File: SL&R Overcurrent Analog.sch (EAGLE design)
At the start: 22 parts, among them IC1 TLC393CPN, IC2 CSLA2CFTH, Q1 SUP75P0307, Q2 SUP75P0307, X1 J1, X2 J2, X3 J3

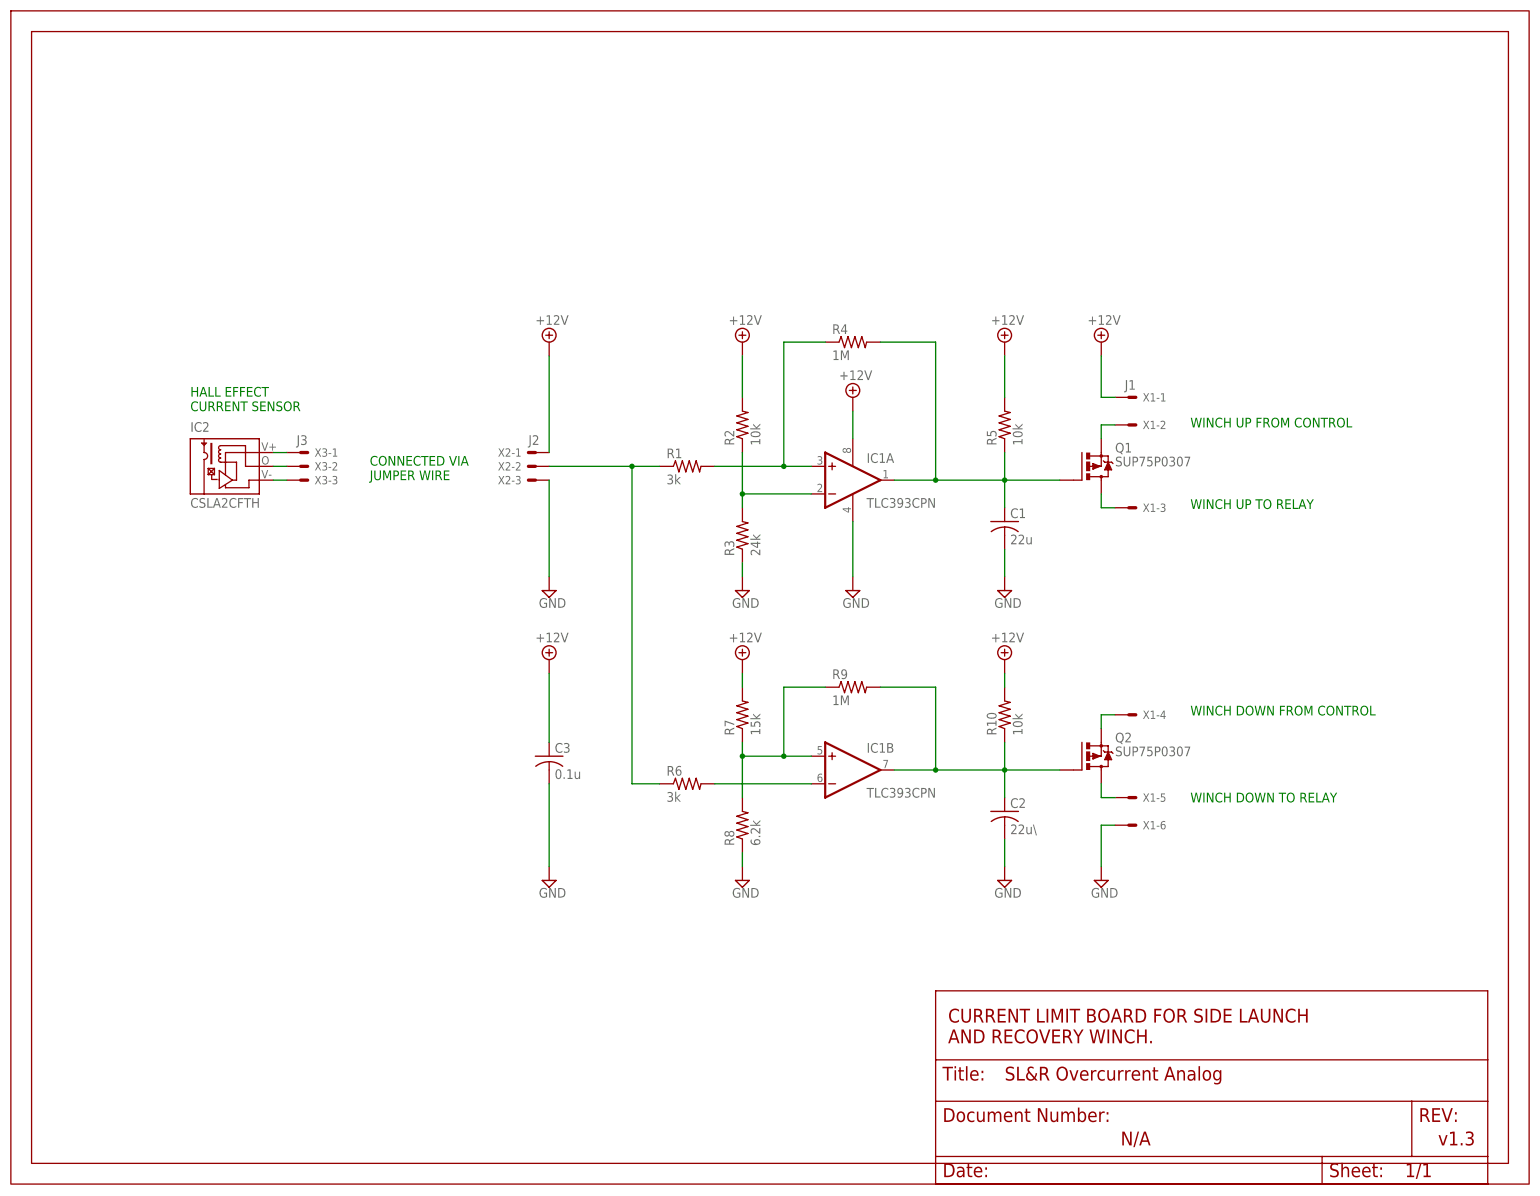
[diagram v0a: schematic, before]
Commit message: Indicators, adjustable limits, test points
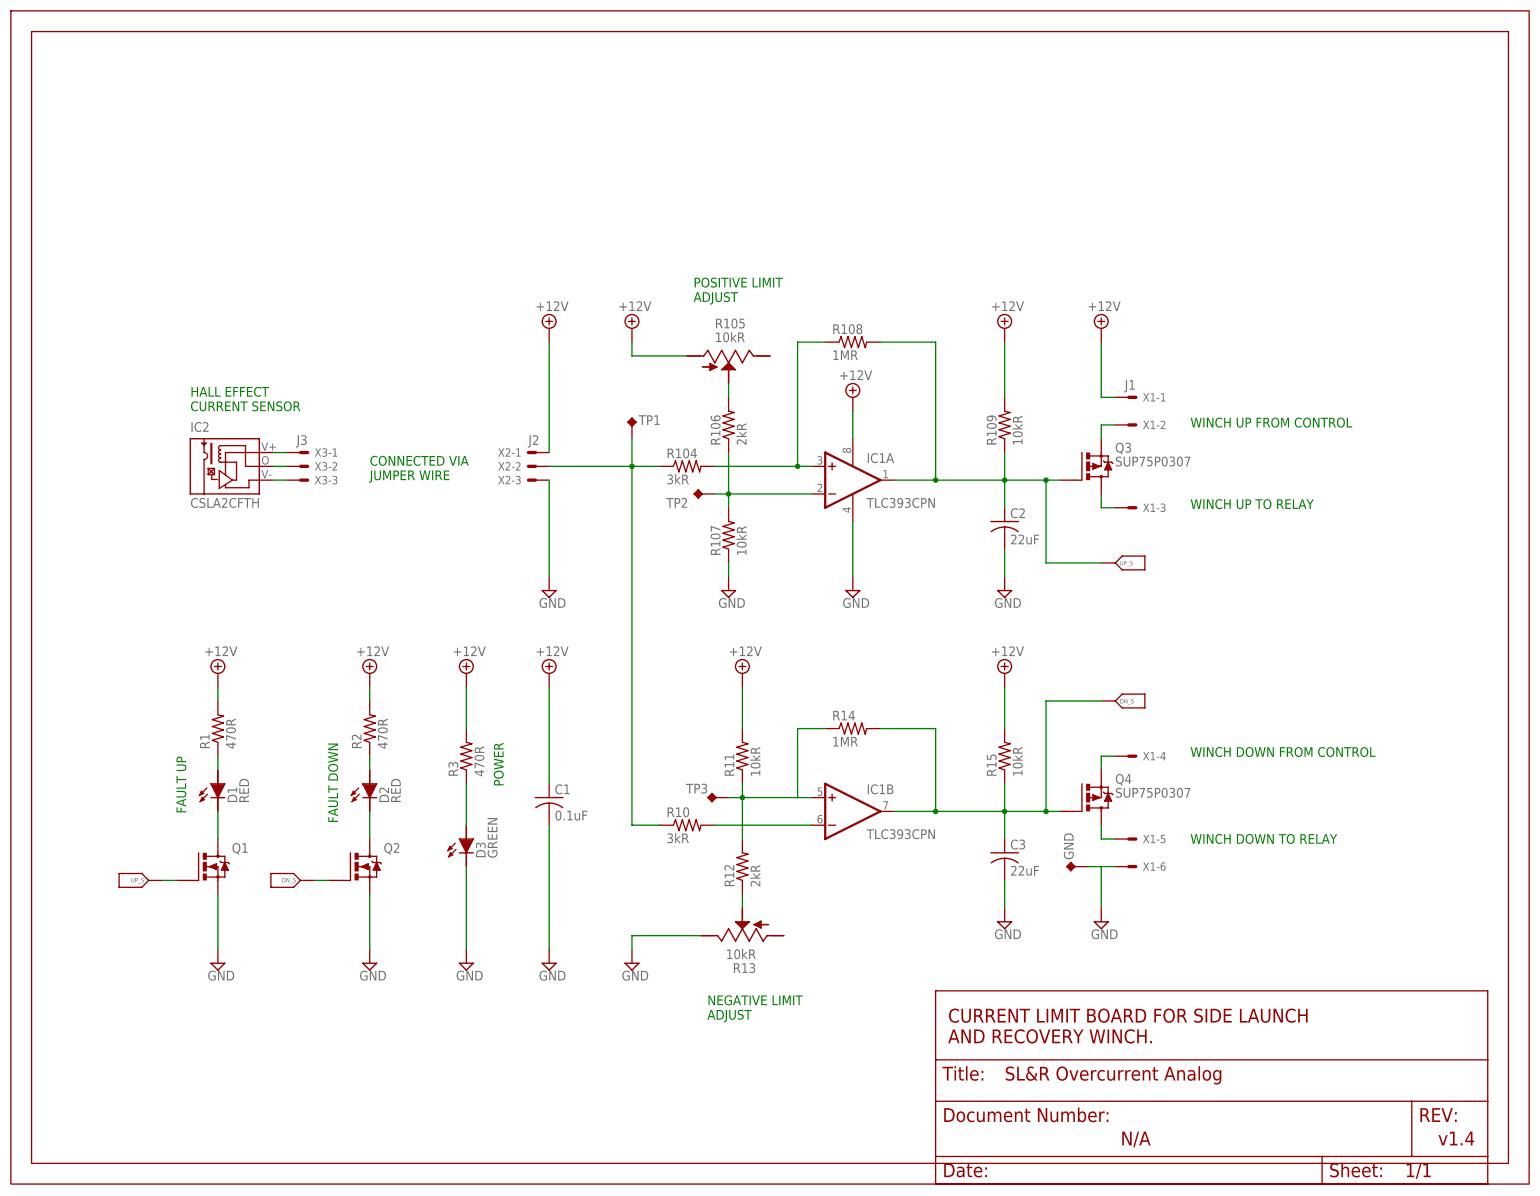
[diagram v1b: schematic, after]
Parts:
- removed R6: 3k, Overcurrent Detect:RESISTOR-US0204/7
- removed R7: 15k, Overcurrent Detect:RESISTOR-US0204/7
- removed R8: 6.2k, Overcurrent Detect:RESISTOR-US0204/7
- removed R9: 1M, Overcurrent Detect:RESISTOR-US0204/7
- added D1, D2: RED, SL&R Overcurrent Analog:LED
- added D3: GREEN, SL&R Overcurrent Analog:LED
- added GND, TP1, TP2, TP3: TEST_POINT, SL&R Overcurrent Analog:TEST_POINT
- added Q3, Q4: SUP75P0307, Overcurrent Detect:SUP75P0307
- added R104: 3kR, Overcurrent Detect:RESISTOR-US0204/7
- added R105, R13: 10kR, SL&R Overcurrent Analog:POT
- added R106, R12: 2kR, Overcurrent Detect:RESISTOR-US0204/7
- added R107, R11, R15: 10kR, Overcurrent Detect:RESISTOR-US0204/7
- added R14: 1MR, Overcurrent Detect:RESISTOR-US0204/7
- C1: value 22u -> 0.1uF; device Overcurrent Detect:CAPACITOR-US025-050X050 -> Overcurrent Detect:CAPACITOR-US
- C2: value 22u\ -> 22uF
- C3: value 0.1u -> 22uF; device Overcurrent Detect:CAPACITOR-US -> Overcurrent Detect:CAPACITOR-US025-050X050
- Q1, Q2: value SUP75P0307 -> (none); device Overcurrent Detect:SUP75P0307 -> SL&R Overcurrent Analog:2N7000
- R1: value 3k -> 470R; device Overcurrent Detect:RESISTOR-US0204/7 -> SL&R Overcurrent Analog:RESISTOR-US0204/7
- R10: value 10k -> 3kR
- R108: value 1M -> 1MR
- R109: value 10k -> 10kR
- R2: value 10k -> 470R; device Overcurrent Detect:RESISTOR-US0204/7 -> SL&R Overcurrent Analog:RESISTOR-US0204/7
- R3: value 24k -> 470R; device Overcurrent Detect:RESISTOR-US0204/7 -> SL&R Overcurrent Analog:RESISTOR-US0204/7
- renumbered R4 to R108, R5 to R109
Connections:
- new net N$16: D1.C, Q1.D
- new net N$17: D2.A, R2.1
- new net N$18: D2.C, Q2.D
- new net N$19: D3.A, R3.1
- new net N$20: R105.2, R106.2
- new net N$22: R12.1, R13.2
- new net N$3: D1.A, R1.1
- net +12V: now also C1.1, R1.2, R105.3, R11.2, R15.2, R3.2; no longer C3.1, R10.2, R7.2
- net GND: now also D3.C, GND.TP, Q1.S, Q2.S, R107.1, R13.1; no longer R3.1, R8.1
- net N$1: now also R104.2; no longer R1.2
- net N$10: now also Q4.S; no longer Q2.S
- net N$11: now also Q4.D; no longer Q2.D
- net N$15: now also R10.1, R104.1, TP1.TP; no longer R1.1, R6.1
- net N$2: now also R106.1, R107.2, TP2.TP; no longer R2.1, R3.2
- net N$4: now also R10.2; no longer R6.2
- net N$5: now also R11.1, R12.2, R14.1, TP3.TP; no longer R7.1, R8.2, R9.1
- net N$6: now also C2.1, Q3.G; no longer C1.1
- net N$7: now also C3.1, Q4.G, R14.2, R15.1; no longer C2.1, R10.1, R9.2
- net N$8: now also Q3.S; no longer Q1.S
- net N$9: now also Q3.D; no longer Q1.D
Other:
- note added: "FAULT DOWN"
- note added: "FAULT UP"
- note added: "NEGATIVE LIMIT ADJUST"
- note added: "POSITIVE LIMIT ADJUST"
- note added: "POWER"
- note added: "v1.4"
- note removed: "v1.3"
- moved on the sheet: C1, C2, C3, IC1B, R1, R10, R2, R3, X1-4, X1-5, X1-6

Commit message: Minor updates
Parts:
- renumbered R104 to R4, R105 to R5, R106 to R6, R107 to R7, R108 to R8, R109 to R9
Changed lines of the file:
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@@
 <part name="IC2" library="Overcurrent Detect" deviceset="CSLA2CF" device="TH"/>
 <part name="IC1" library="Overcurrent Detect" deviceset="TLC393CP" device="N"/>
-<part name="R104" library="Overcurrent Detect" deviceset="RESISTOR-US" device="0204/7" value="3kR"/>
-<part name="R106" library="Overcurrent Detect" deviceset="RESISTOR-US" device="0204/7" value="2kR"/>
-<part name="R108" library="Overcurrent Detect" deviceset="RESISTOR-US" device="0204/7" value="1MR"/>
-<part name="R109" library="Overcurrent Detect" deviceset="RESISTOR-US" device="0204/7" value="10kR"/>
+<part name="R4" library="Overcurrent Detect" deviceset="RESISTOR-US" device="0204/7" value="3kR"/>
+<part name="R6" library="Overcurrent Detect" deviceset="RESISTOR-US" device="0204/7" value="2kR"/>
+<part name="R8" library="Overcurrent Detect" deviceset="RESISTOR-US" device="0204/7" value="1MR"/>
+<part name="R9" library="Overcurrent Detect" deviceset="RESISTOR-US" device="0204/7" value="10kR"/>
 <part name="R10" library="Overcurrent Detect" deviceset="RESISTOR-US" device="0204/7" value="3kR"/>
 <part name="R12" library="Overcurrent Detect" deviceset="RESISTOR-US" device="0204/7" value="2kR"/>
@@
 <part name="LABEL3" library="SL&amp;R Overcurrent Analog" deviceset="WIRE_LABEL" device="" value="UP_S"/>
 <part name="LABEL4" library="SL&amp;R Overcurrent Analog" deviceset="WIRE_LABEL" device="" value="DN_S"/>
-<part name="R105" library="SL&amp;R Overcurrent Analog" deviceset="POT" device="" value="10kR"/>
+<part name="R5" library="SL&amp;R Overcurrent Analog" deviceset="POT" device="" value="10kR"/>
 <part name="R13" library="SL&amp;R Overcurrent Analog" deviceset="POT" device="" value="10kR"/>
 <part name="Q1" library="SL&amp;R Overcurrent Analog" deviceset="2N7000" device=""/>
 <part name="Q2" library="SL&amp;R Overcurrent Analog" deviceset="2N7000" device=""/>
-<part name="R107" library="Overcurrent Detect" deviceset="RESISTOR-US" device="0204/7" value="10kR"/>
+<part name="R7" library="Overcurrent Detect" deviceset="RESISTOR-US" device="0204/7" value="10kR"/>
 <part name="R11" library="Overcurrent Detect" deviceset="RESISTOR-US" device="0204/7" value="10kR"/>
 </parts>
@@
 <instance part="IC1" gate="A" x="55.88" y="81.28"/>
 <instance part="IC1" gate="B" x="55.88" y="20.32"/>
-<instance part="R104" gate="G$1" x="25.4" y="83.82"/>
-<instance part="R106" gate="G$1" x="33.02" y="91.44" rot="R90"/>
-<instance part="R108" gate="G$1" x="55.88" y="106.68"/>
-<instance part="R109" gate="G$1" x="83.82" y="91.44" rot="R90"/>
+<instance part="R4" gate="G$1" x="25.4" y="83.82"/>
+<instance part="R6" gate="G$1" x="33.02" y="91.44" rot="R90"/>
+<instance part="R8" gate="G$1" x="55.88" y="106.68"/>
+<instance part="R9" gate="G$1" x="83.82" y="91.44" rot="R90"/>
 <instance part="R10" gate="G$1" x="25.4" y="17.78"/>
 <instance part="R12" gate="G$1" x="35.56" y="10.16" rot="R90"/>
@@
 <instance part="LABEL3" gate="G$1" x="-78.74" y="7.62"/>
 <instance part="LABEL4" gate="G$1" x="-50.8" y="7.62"/>
-<instance part="R105" gate="G$1" x="33.02" y="104.14" rot="R270"/>
+<instance part="R5" gate="G$1" x="33.02" y="104.14" rot="R270"/>
 <instance part="R13" gate="G$1" x="35.56" y="-2.54" rot="R90"/>
 <instance part="Q1" gate="G$1" x="-63.5" y="10.16"/>
 <instance part="Q2" gate="G$1" x="-35.56" y="10.16"/>
-<instance part="R107" gate="G$1" x="33.02" y="71.12" rot="R90"/>
+<instance part="R7" gate="G$1" x="33.02" y="71.12" rot="R90"/>
 <instance part="R11" gate="G$1" x="35.56" y="30.48" rot="R90"/>
 </instances>
@@
 </segment>
 <segment>
-<pinref part="R109" gate="G$1" pin="2"/>
+<pinref part="R9" gate="G$1" pin="2"/>
 <pinref part="SUPPLY7" gate="+12V" pin="+12V"/>
 <wire x1="83.82" y1="96.52" x2="83.82" y2="106.68" width="0.1524" layer="91"/>
@@
 <segment>
 <pinref part="SUPPLY3" gate="+12V" pin="+12V"/>
-<pinref part="R105" gate="G$1" pin="3"/>
+<pinref part="R5" gate="G$1" pin="3"/>
 <wire x1="15.24" y1="106.68" x2="15.24" y2="104.14" width="0.1524" layer="91"/>
 <wire x1="15.24" y1="104.14" x2="25.4" y2="104.14" width="0.1524" layer="91"/>
@@
 </segment>
 <segment>
-<pinref part="R107" gate="G$1" pin="1"/>
+<pinref part="R7" gate="G$1" pin="1"/>
 <pinref part="SUPPLY5" gate="GND" pin="GND"/>
 <wire x1="33.02" y1="66.04" x2="33.02" y2="63.5" width="0.1524" layer="91"/>
@@
 <net name="N$1" class="0">
 <segment>
-<pinref part="R104" gate="G$1" pin="2"/>
+<pinref part="R4" gate="G$1" pin="2"/>
 <pinref part="IC1" gate="A" pin="+IN"/>
 <wire x1="30.48" y1="83.82" x2="45.72" y2="83.82" width="0.1524" layer="91"/>
-<pinref part="R108" gate="G$1" pin="1"/>
+<pinref part="R8" gate="G$1" pin="1"/>
 <wire x1="45.72" y1="83.82" x2="48.26" y2="83.82" width="0.1524" layer="91"/>
 <wire x1="50.8" y1="106.68" x2="45.72" y2="106.68" width="0.1524" layer="91"/>
@@
 <wire x1="48.26" y1="78.74" x2="33.02" y2="78.74" width="0.1524" layer="91"/>
 <pinref part="TP2" gate="G$1" pin="TP"/>
-<pinref part="R106" gate="G$1" pin="1"/>
-<pinref part="R107" gate="G$1" pin="2"/>
+<pinref part="R6" gate="G$1" pin="1"/>
+<pinref part="R7" gate="G$1" pin="2"/>
 <wire x1="33.02" y1="78.74" x2="30.48" y2="78.74" width="0.1524" layer="91"/>
 <wire x1="33.02" y1="86.36" x2="33.02" y2="78.74" width="0.1524" layer="91"/>
@@
 <net name="N$6" class="0">
 <segment>
-<pinref part="R108" gate="G$1" pin="2"/>
+<pinref part="R8" gate="G$1" pin="2"/>
 <wire x1="60.96" y1="106.68" x2="71.12" y2="106.68" width="0.1524" layer="91"/>
 <wire x1="71.12" y1="106.68" x2="71.12" y2="81.28" width="0.1524" layer="91"/>
@@
 <wire x1="71.12" y1="81.28" x2="83.82" y2="81.28" width="0.1524" layer="91"/>
 <junction x="71.12" y="81.28"/>
-<pinref part="R109" gate="G$1" pin="1"/>
+<pinref part="R9" gate="G$1" pin="1"/>
 <wire x1="83.82" y1="81.28" x2="91.44" y2="81.28" width="0.1524" layer="91"/>
 <wire x1="91.44" y1="81.28" x2="93.98" y2="81.28" width="0.1524" layer="91"/>
@@
 <wire x1="20.32" y1="17.78" x2="15.24" y2="17.78" width="0.1524" layer="91"/>
 <wire x1="15.24" y1="17.78" x2="15.24" y2="83.82" width="0.1524" layer="91"/>
-<pinref part="R104" gate="G$1" pin="1"/>
+<pinref part="R4" gate="G$1" pin="1"/>
 <wire x1="15.24" y1="83.82" x2="20.32" y2="83.82" width="0.1524" layer="91"/>
 <pinref part="X2" gate="-2" pin="S"/>
@@
 <net name="N$20" class="0">
 <segment>
-<pinref part="R105" gate="G$1" pin="2"/>
-<pinref part="R106" gate="G$1" pin="2"/>
+<pinref part="R5" gate="G$1" pin="2"/>
+<pinref part="R6" gate="G$1" pin="2"/>
 <wire x1="33.02" y1="99.06" x2="33.02" y2="96.52" width="0.1524" layer="91"/>
 </segment>
